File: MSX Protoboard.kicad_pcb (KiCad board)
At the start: 2 copper layers, 103 x 66 mm, 806 parts

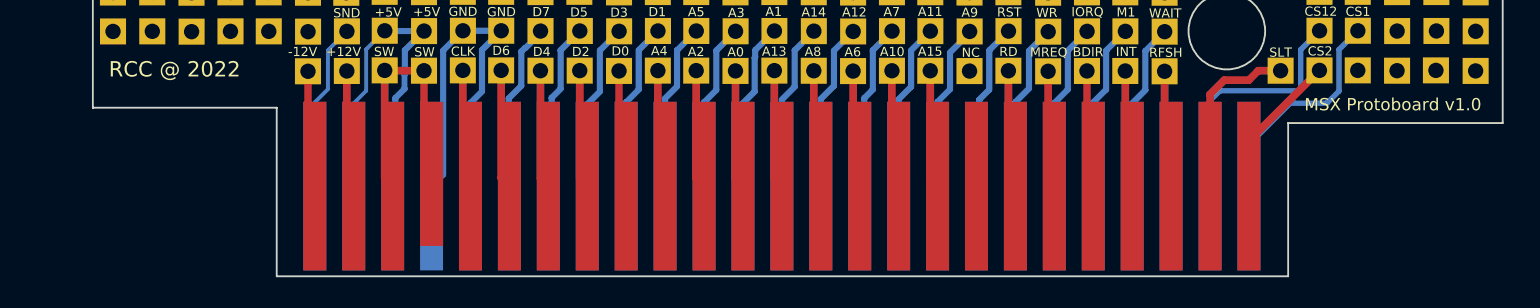
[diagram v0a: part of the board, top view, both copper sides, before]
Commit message: Adjusted width of edge connector to 64mm
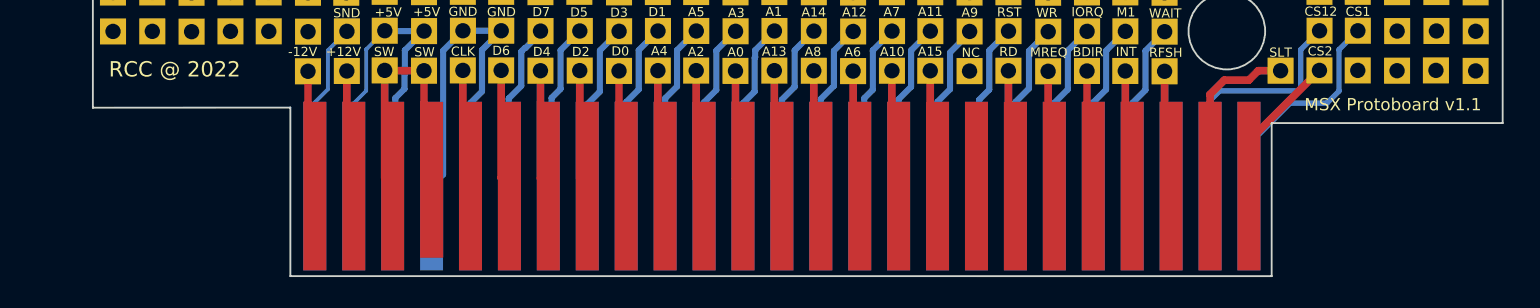
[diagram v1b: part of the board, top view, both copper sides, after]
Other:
- outline, holes or cut-outs redrawn
- board text added: "MSX Protoboard v1.1"
- board text removed: "MSX Protoboard v1.0"
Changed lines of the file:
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@@
   (title_block
     (title "MSX Protoboard")
-    (date "2022-12-20")
-    (rev "1.0")
+    (date "2023-02-26")
+    (rev "1.1")
     (company "RCC")
   )
@@
       (effects (font (size 1 1) (thickness 0.15)))
     )
+    (fp_line (start -49.66 13.4) (end -49.66 -30.6) (layer "Edge.Cuts") (width 0.12))
+    (fp_line (start -25.772154 35.388435) (end 38.265868 35.390806) (layer "Edge.Cuts") (width 0.12))
+    (fp_line (start 38.263821 25.400771) (end 53.34 25.4) (layer "Edge.Cuts") (width 0.12))
     (fp_line (start -38.66 13.4) (end -38.66 24.4) (layer "Edge.Cuts") (width 0.12))
-    (fp_line (start -26.66 35.4) (end -26.66 24.4) (layer "Edge.Cuts") (width 0.12))
-    (fp_line (start -26.66 35.4) (end 39.34 35.4) (layer "Edge.Cuts") (width 0.12))
-    (fp_line (start 39.34 25.4) (end 53.34 25.4) (layer "Edge.Cuts") (width 0.12))
     (fp_line (start 53.34 -30.6) (end -49.66 -30.6) (layer "Edge.Cuts") (width 0.12))
-    (fp_line (start 39.34 25.4) (end 39.34 35.4) (layer "Edge.Cuts") (width 0.12))
-    (fp_line (start -49.66 13.4) (end -49.66 -30.6) (layer "Edge.Cuts") (width 0.12))
+    (fp_line (start -38.66 24.4) (end -25.772154 24.388435) (layer "Edge.Cuts") (width 0.12))
     (fp_line (start -49.66 13.4) (end -38.66 13.4) (layer "Edge.Cuts") (width 0.12))
+    (fp_line (start -25.772154 35.388435) (end -25.772154 24.388435) (layer "Edge.Cuts") (width 0.12))
     (fp_line (start 53.34 -30.6) (end 53.34 25.4) (layer "Edge.Cuts") (width 0.12))
-    (fp_line (start -38.66 24.4) (end -26.66 24.4) (layer "Edge.Cuts") (width 0.12))
-    (fp_circle (center 35.34 19.4) (end 37.84 19.4) (layer "Edge.Cuts") (width 0.12) (fill none))
+    (fp_line (start 38.263821 25.400771) (end 38.265868 35.390806) (layer "Edge.Cuts") (width 0.12))
     (fp_circle (center -21.66 13.4) (end -19.16 13.4) (layer "Edge.Cuts") (width 0.12) (fill none))
+    (fp_circle (center 35.34 19.4) (end 37.84 19.4) (layer "Edge.Cuts") (width 0.12) (fill none))
     (pad "1" connect rect (at 36.782025 29.514405) (size 1.5 11) (layers "B.Cu" "B.Mask")
       (net 9 "{slash}CS1") (pinfunction "/CS1") (pintype "output"))
@@
     (pad "43" connect rect (at -16.557975 29.514405) (size 1.5 11) (layers "B.Cu" "B.Mask")
       (net 3 "GNDREF") (pinfunction "GND") (pintype "output"))
-    (pad "44" connect rect (at -16.553954 28.716024) (size 1.50804 9.403238) (layers "F.Cu" "F.Mask")
+    (pad "44" connect rect (at -16.552858 29.102863) (size 1.510191 10.176916) (layers "F.Cu" "F.Mask")
       (net 47 "SW1") (pinfunction "SW1") (pintype "output"))
     (pad "45" connect rect (at -19.097975 29.514405) (size 1.5 11) (layers "B.Cu" "B.Mask")
@@
     (effects (font (size 0.6 0.6) (thickness 0.125)))
   )
-  (gr_text "MSX Protoboard v1.0" (at 149.5 82.2) (layer "F.SilkS")
+  (gr_text "MSX Protoboard v1.1" (at 149.5 82.2) (layer "F.SilkS")
     (effects (font (size 0.8 0.8) (thickness 0.15)))
   )

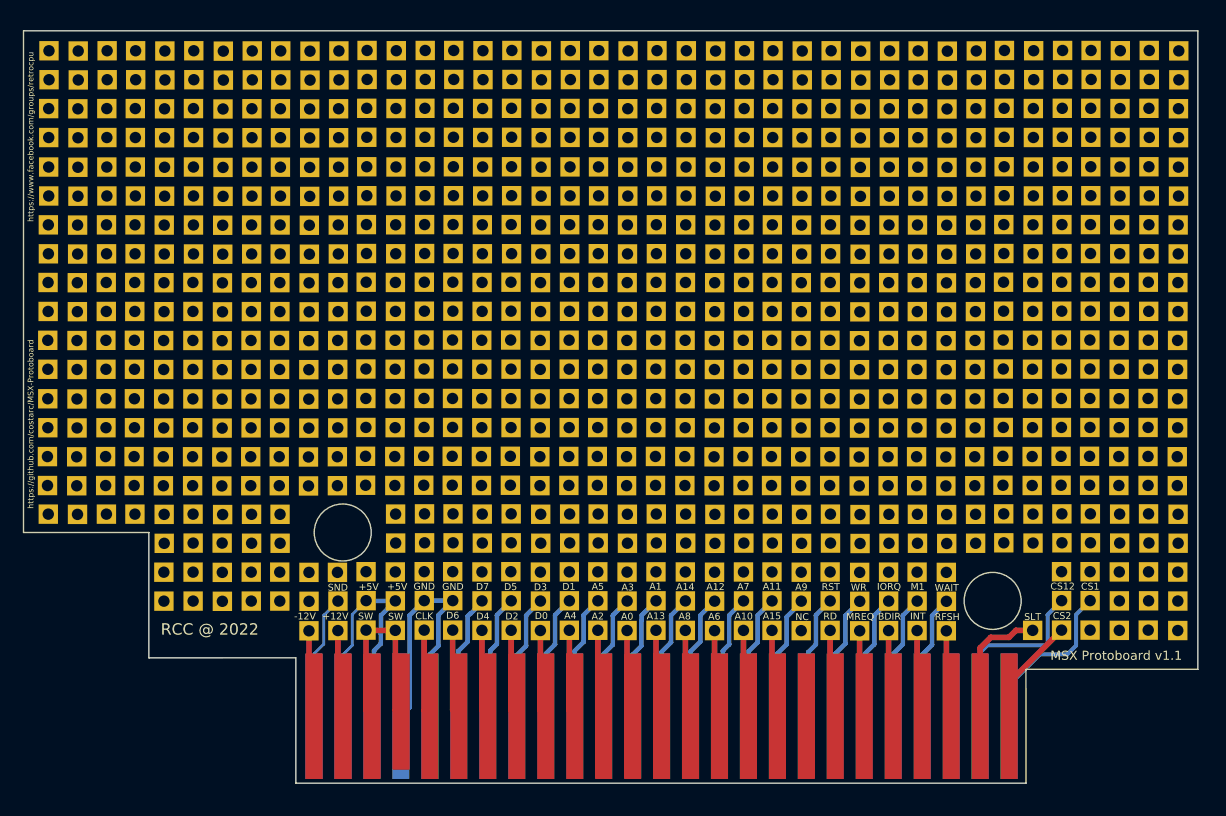
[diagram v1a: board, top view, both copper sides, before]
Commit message: Update pcb footprint
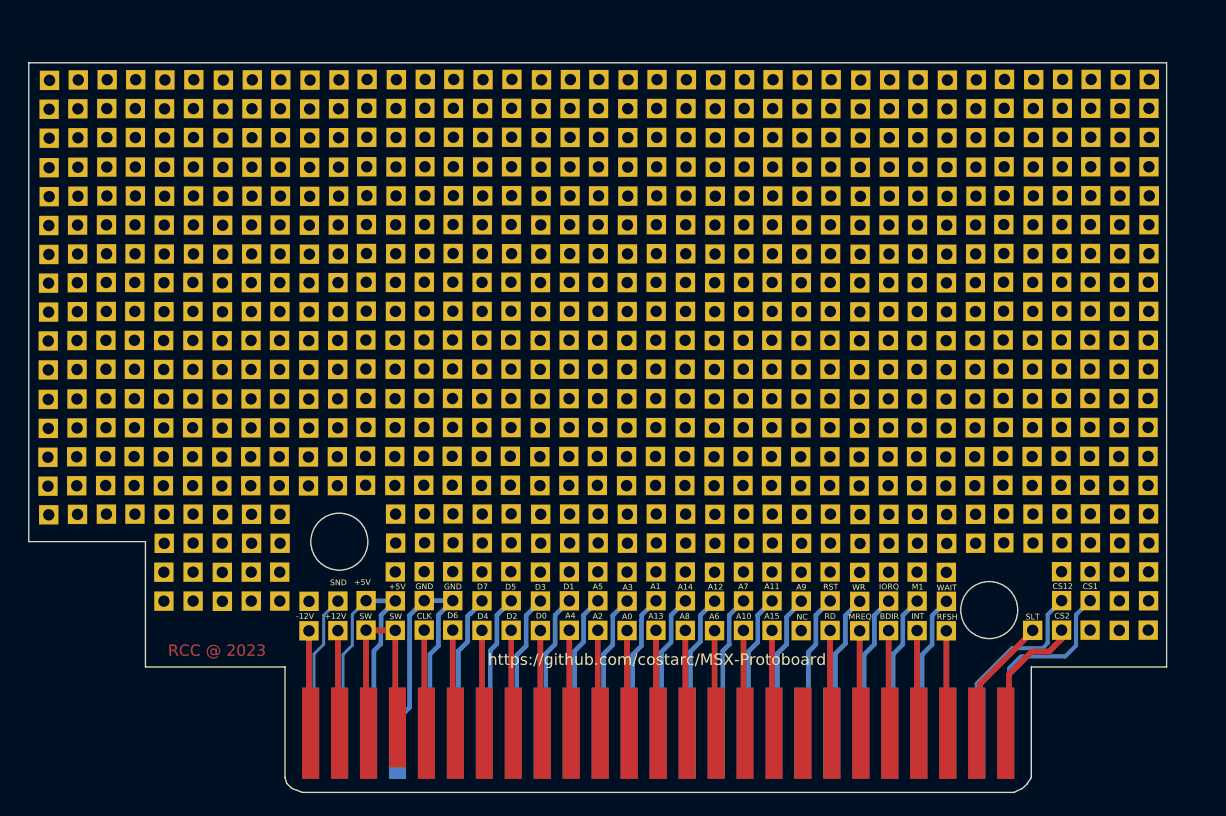
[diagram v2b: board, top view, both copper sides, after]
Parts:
- removed the ? at (114.4, 29.2)
- removed the ? at (55.8, 47.0)
- removed the ? at (78.7, 74.9)
- removed the ? at (55.9, 29.2)
- removed the ? at (61.0, 29.2)
- removed the ? at (55.8, 52.0)
- removed the ? at (63.5, 29.2)
- removed the ? at (88.9, 29.1)
- removed the ? at (99.1, 29.2)
- removed the ? at (55.8, 67.3)
- removed the ? at (55.8, 54.5)
- removed the ? at (155.0, 34.2)
- removed the ? at (137.2, 29.2)
- removed the ? at (147.3, 29.1)
- removed the ? at (134.7, 29.2)
- removed the ? at (129.6, 29.2)
- removed the ? at (132.1, 29.2)
- removed the ? at (142.3, 29.1)
- removed the ? at (127.1, 29.2)
- removed the ? at (154.9, 52.0)
- removed the ? at (81.2, 74.9)
- removed the ? at (149.9, 29.1)
- removed the ? at (154.9, 72.3)
- removed the ? at (55.8, 59.7)
- removed the ? at (86.4, 29.1)
- removed the ? at (154.9, 74.9)
- removed the ? at (55.9, 34.2)
- removed the ? at (55.8, 49.5)
- removed the ? at (78.8, 29.2)
- removed the ? at (155.0, 39.4)
- removed the ? at (55.8, 64.7)
- removed the ? at (154.9, 47.0)
- removed the ? at (111.8, 29.2)
- removed the ? at (154.9, 62.2)
- removed the ? at (154.9, 57.1)
- removed the ? at (55.8, 57.1)
- removed the ? at (154.9, 49.5)
- removed the ? at (155.0, 41.9)
- removed the ? at (83.8, 29.1)
- removed the ? at (154.9, 54.6)
- removed the ? at (55.9, 41.9)
- removed the ? at (66.1, 29.2)
- removed the ? at (106.7, 29.2)
- removed the ? at (94.0, 29.1)
- removed the ? at (91.4, 29.1)
- removed the ? at (101.6, 29.1)
- removed the ? at (154.9, 64.8)
- removed the ? at (96.5, 29.1)
- removed the ? at (71.2, 29.2)
- removed the ? at (155.0, 31.7)
- removed the ? at (155.0, 36.8)
- removed the ? at (122.0, 29.2)
- removed the ? at (154.9, 77.4)
- removed the ? at (119.4, 29.2)
- removed the ? at (55.8, 44.4)
- removed the ? at (55.9, 39.3)
- removed the ? at (154.9, 80.0)
- removed the ? at (144.8, 29.1)
- removed the ? at (109.2, 29.1)
- removed the ? at (58.5, 29.2)
- removed the ? at (154.9, 69.8)
- removed the ? at (152.4, 29.1)
- removed the ? at (68.6, 29.2)
- removed the ? at (55.9, 31.7)
- removed the ? at (155.0, 29.2)
- removed the ? at (83.7, 74.8)
- removed the ? at (124.5, 29.2)
- removed the ? at (154.9, 67.3)
- removed the ? at (81.3, 29.2)
- removed the ? at (139.7, 29.1)
- removed the ? at (154.9, 44.4)
- removed the ? at (55.8, 69.8)
- removed the ? at (104.1, 29.1)
- removed the ? at (154.9, 59.7)
- removed the ? at (55.8, 62.2)
- removed the ? at (76.2, 29.2)
- removed the ? at (73.7, 29.2)
- removed the ? at (55.9, 36.8)
- removed the ? at (116.9, 29.2)
- added ?: , , F.Cu at (55.8, 62.3)
- added ?: , , F.Cu at (55.9, 39.4)
- added ?: , , F.Cu at (55.8, 67.3)
- added ?: , , F.Cu at (55.9, 49.5)
- added ?: , , F.Cu at (55.8, 59.7)
- added ?: , , F.Cu at (55.9, 69.8)
- added ?: , , F.Cu at (55.9, 47.0)
- added ?: , , F.Cu at (55.9, 31.7)
- added ?: , , F.Cu at (55.8, 57.1)
- added ?: , , F.Cu at (55.8, 64.8)
- added ?: , , F.Cu at (55.8, 54.6)
- added ?: , , F.Cu at (55.9, 52.1)
- added ?: , , F.Cu at (55.9, 36.8)
- added ?: , , F.Cu at (55.9, 41.9)
- added ?: , , F.Cu at (55.9, 34.3)
- added ?: , , F.Cu at (55.9, 44.5)
- CONN1: footprint Roni Footprints:MSX_CART_SW -> Roni Footprints:MSX_CART_SW_Official
- moved CONN1 0.86 mm to (103.0, 58.8)
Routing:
- net /SLTSL: track 11.2 -> 9.57 mm
- net /CS12: track 16.1 -> 14.9 mm
- net /CS2: track 9.46 -> 10.4 mm
- net /CS1: track 14.5 -> 15.3 mm
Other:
- board size 103 x 66 mm -> 99.8 x 64 mm
- board text removed: "MSX Protoboard v1.1"
- board text removed: "RCC @ 2022"
- board text removed: "https://www.facebook.com/groups/retrocpu"
